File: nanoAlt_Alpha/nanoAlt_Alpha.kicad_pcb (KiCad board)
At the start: 4 copper layers, 12 x 14 mm, 18 parts, among them IC1 MS563702BA03-50, J1 AVR_SPI_PROG_3X2TESTPOINTS, U1 ATTINY24A-CCU

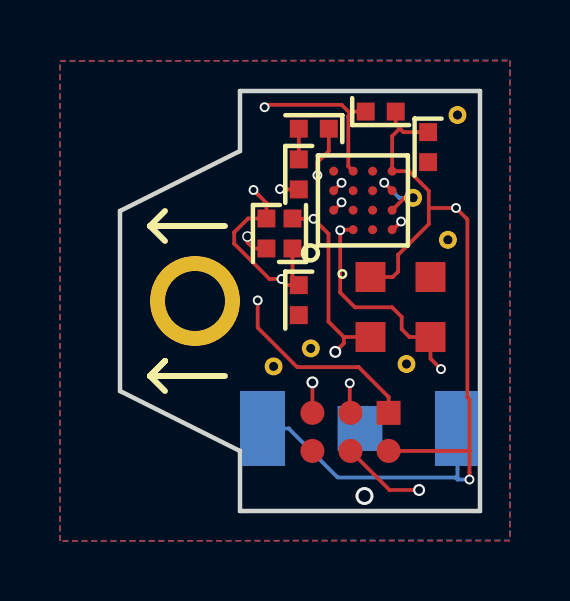
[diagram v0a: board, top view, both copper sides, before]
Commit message: Reroute for 2 layers
Signed-off-by: Pierros Papadeas <pierros@papadeas.gr>
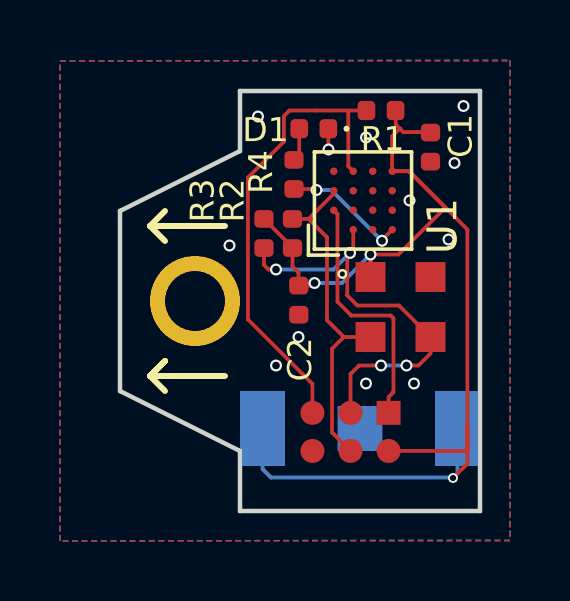
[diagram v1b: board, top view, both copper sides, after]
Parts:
- removed V** (x6): VIA-0.6mm, My_VIAS:VIA-0.6mm
- C1, C2: value 100nF_0402 -> 100n; footprint My_PASSIVES:0402 -> Capacitor_SMD:C_0402_1005Metric
- D1: footprint My_PASSIVES:0402 -> LED_SMD:LED_0402_1005Metric
- R1, R2, R3: value 10KOHM-0402 -> 10K; footprint My_PASSIVES:0402 -> Resistor_SMD:R_0402_1005Metric
- R4: value 33OHM-0402 -> 33; footprint My_PASSIVES:0402 -> Resistor_SMD:R_0402_1005Metric
- U1: value ATTINY24A-CCU -> ATtiny24A-CCU; footprint My_IC:UFBGA_15CC1 -> Package_BGA:UFBGA-15_3.0x3.0mm_Layout4x4_P0.65mm
- moved U1 1.37 mm to (139.1, 102.7)
- moved R4 0.16 mm to (136.8, 101.8), turned to 90 degrees
- moved R3 0.08 mm to (135.8, 103.7)
- moved C1 0.08 mm to (141.3, 100.9)
- turned R1 to 180 degrees
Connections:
- R1 pad 1: /RST -> +BATT
- R1 pad 2: +BATT -> /RST
- R4 pad 1: Net-(D1-Pad2) -> Net-(R4-Pad1)
- R4 pad 2: Net-(R4-Pad2) -> Net-(D1-Pad2)
- U1 pad D1: Net-(R4-Pad2) -> Net-(R4-Pad1)
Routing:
- net /RST: track 22.8 -> 16.2 mm, vias 3 -> 0
- net Net-(R4-Pad2): track 6.52 -> 0.00 mm, vias 2 -> 0
- net GND: track 6.58 -> 0.71 mm, vias 2 -> 12
- net /MOSI: track 17.1 -> 11.4 mm, vias 4 -> 0
- net /MISO: track 12.9 -> 8.43 mm, vias 2 -> 0
- net Net-(R4-Pad1): track 0.00 -> 4.16 mm, vias 0 -> 2
- net +BATT: track 44.5 -> 40.5 mm, vias 4 -> 3
- net /SCL: track 16.0 -> 14.2 mm
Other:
- copper layers 4 -> 2
